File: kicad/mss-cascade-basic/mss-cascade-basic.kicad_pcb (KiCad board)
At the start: 2 copper layers, 73.7 x 38.1 mm, 36 parts, among them J1 Screw_Terminal_01x02, J2 AVR-ISP, J3 8P8C, J4 8P8C, SW1 FSM4JSMATR, T1 PE-51687, U1 AP7381-33Y, U2 INA180A4, U3 ATtiny85-20S, U4 TLP241A

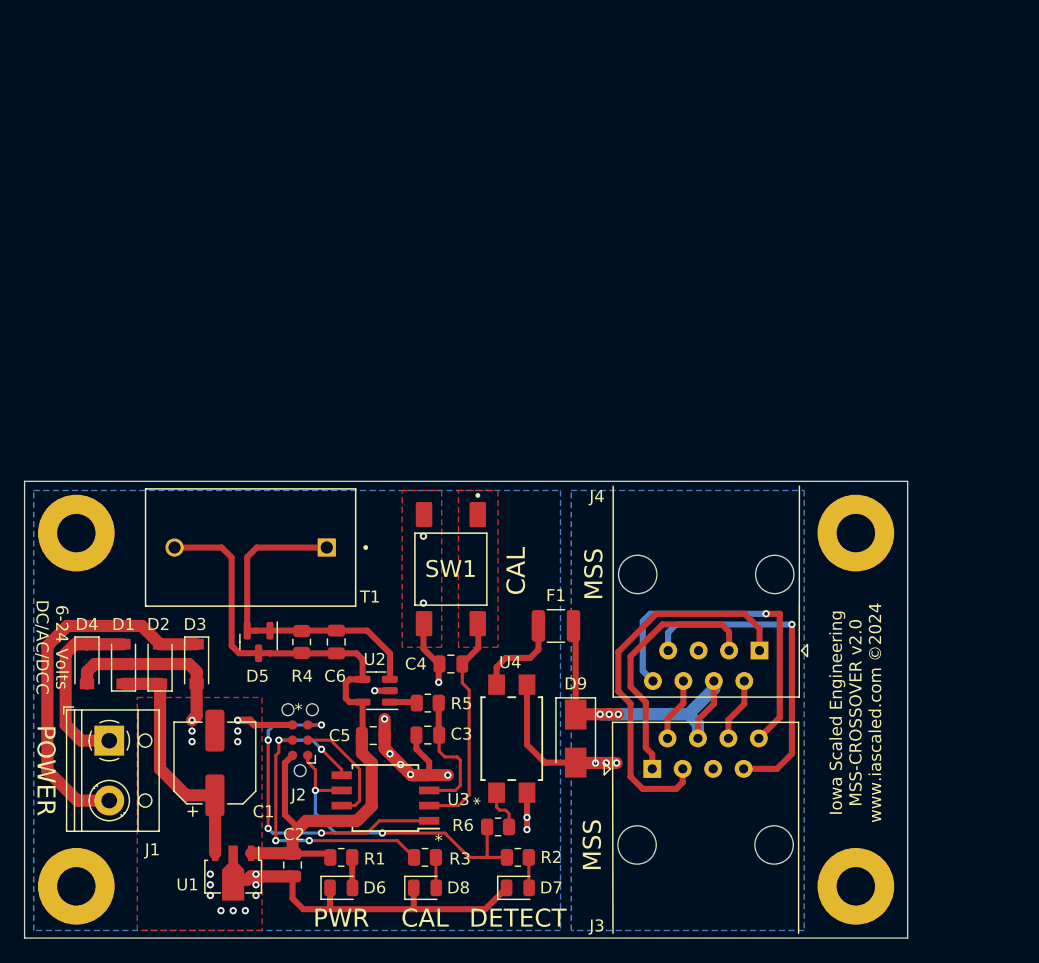
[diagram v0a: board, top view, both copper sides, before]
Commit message: Initial PCB layout for basic cascade
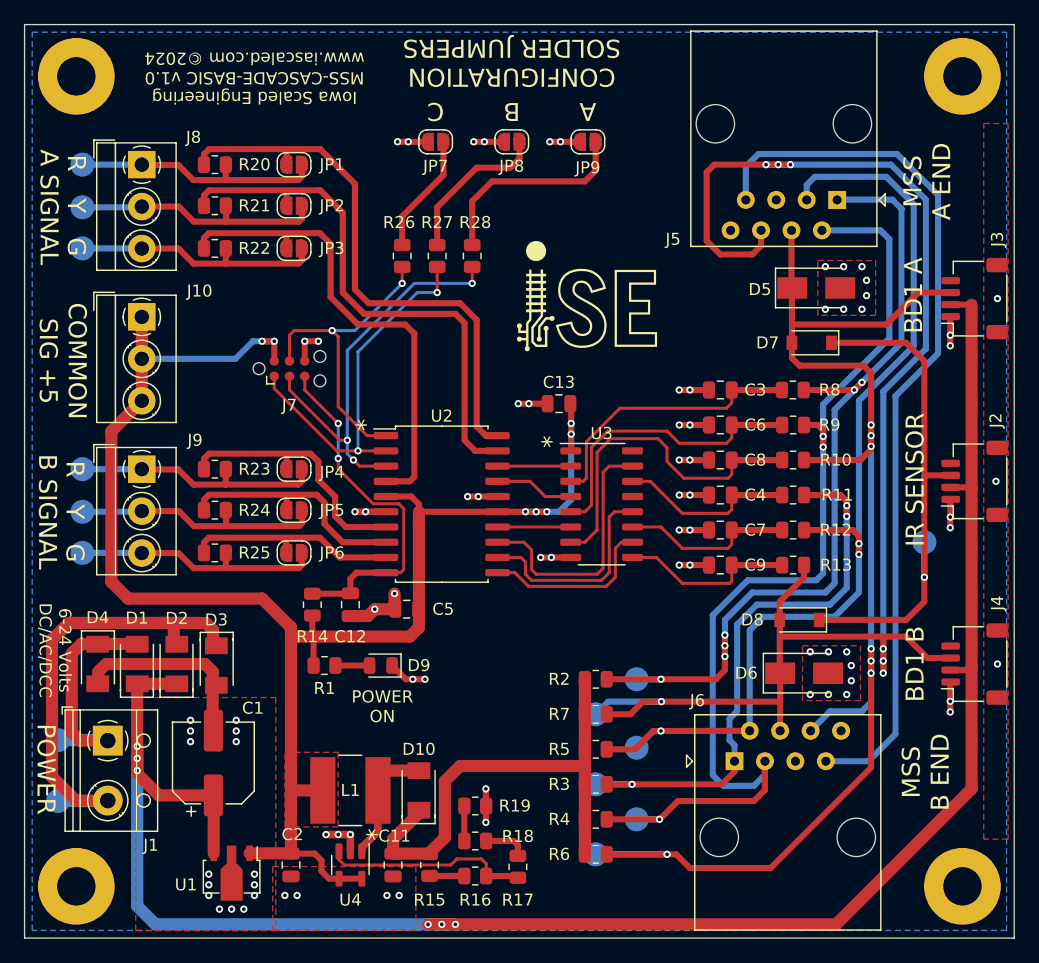
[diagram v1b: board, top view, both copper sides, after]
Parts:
- removed F1: 1210L020WR, Resistor_SMD:R_1210_3225Metric
- removed SW1: FSM4JSMATR, ISE_Generic:TE_FSM4JSMA
- removed T1: PE-51687, ISE_Generic:XFMR_PE-51687
- added C11: 10uF, Capacitor_SMD:C_0805_2012Metric, F.Cu at (56.1, 185.7)
- added C12: 1uF, Capacitor_SMD:C_0805_2012Metric, F.Cu at (52.6, 164.0)
- added C13: 0.1uF, Capacitor_SMD:C_0805_2012Metric, F.Cu at (70.0, 147.2)
- added C7: 0.1uF, Capacitor_SMD:C_0805_2012Metric, F.Cu at (83.4, 157.7)
- added C8: 0.1uF, Capacitor_SMD:C_0805_2012Metric, F.Cu at (83.4, 151.9)
- added C9: 0.1uF, Capacitor_SMD:C_0805_2012Metric, F.Cu at (83.4, 160.7)
- added D10: CDBM140G, ISE_Generic:SOD-123T, F.Cu at (58.3, 179.5)
- added J10: Screw_Terminal_01x02, TerminalBlock_MetzConnect:TerminalBlock_MetzConnect_Type059_RT06303HBWC_1x03_P3.50mm_Horizontal, F.Cu at (35.2, 140.0)
- added J5: 8P8C, Connector_RJ:RJ45_Amphenol_54602-x08_Horizontal, F.Cu at (93.2, 130.2)
- added J6: 8P8C, Connector_RJ:RJ45_Amphenol_54602-x08_Horizontal, F.Cu at (84.6, 177.0)
- added J7: AVR-ISP, Connector:Tag-Connect_TC2030-IDC-NL_2x03_P1.27mm_Vertical, F.Cu at (47.5, 144.3)
- added J8: Screw_Terminal_01x02, TerminalBlock_MetzConnect:TerminalBlock_MetzConnect_Type059_RT06303HBWC_1x03_P3.50mm_Horizontal, F.Cu at (35.2, 127.3)
- added J9: Screw_Terminal_01x02, TerminalBlock_MetzConnect:TerminalBlock_MetzConnect_Type059_RT06303HBWC_1x03_P3.50mm_Horizontal, F.Cu at (35.2, 152.7)
- added JP1: SolderJumper_2_Open, Jumper:SolderJumper-2_P1.3mm_Open_RoundedPad1.0x1.5mm, F.Cu at (47.9, 127.3)
- added JP2: SolderJumper_2_Open, Jumper:SolderJumper-2_P1.3mm_Open_RoundedPad1.0x1.5mm, F.Cu at (47.9, 130.7)
- added JP3: SolderJumper_2_Open, Jumper:SolderJumper-2_P1.3mm_Open_RoundedPad1.0x1.5mm, F.Cu at (47.9, 134.2)
- added JP4: SolderJumper_2_Open, Jumper:SolderJumper-2_P1.3mm_Open_RoundedPad1.0x1.5mm, F.Cu at (47.9, 152.7)
- added JP5: SolderJumper_2_Open, Jumper:SolderJumper-2_P1.3mm_Open_RoundedPad1.0x1.5mm, F.Cu at (47.9, 156.1)
- added JP6: SolderJumper_2_Open, Jumper:SolderJumper-2_P1.3mm_Open_RoundedPad1.0x1.5mm, F.Cu at (47.9, 159.6)
- added JP7: SolderJumper_2_Open, Jumper:SolderJumper-2_P1.3mm_Open_RoundedPad1.0x1.5mm, F.Cu at (59.7, 125.3)
- added JP8: SolderJumper_2_Open, Jumper:SolderJumper-2_P1.3mm_Open_RoundedPad1.0x1.5mm, F.Cu at (66.0, 125.3)
- added JP9: SolderJumper_2_Open, Jumper:SolderJumper-2_P1.3mm_Open_RoundedPad1.0x1.5mm, F.Cu at (72.4, 125.3)
- added L1: 4.7uH, ISE_UltraLibrarian:MSS6132-xxxMLC, F.Cu at (52.6, 179.5)
- added R10: 10k, Resistor_SMD:R_0805_2012Metric, F.Cu at (89.5, 151.9)
- added R11: 10k, Resistor_SMD:R_0805_2012Metric, F.Cu at (89.5, 154.8)
- added R12: 10k, Resistor_SMD:R_0805_2012Metric, F.Cu at (89.5, 157.7)
- added R13: 10k, Resistor_SMD:R_0805_2012Metric, F.Cu at (89.5, 160.7)
- added R14: 10k, Resistor_SMD:R_0805_2012Metric, F.Cu at (49.4, 164.0)
- added R15: 10k, Resistor_SMD:R_0805_2012Metric, F.Cu at (59.2, 185.7)
- added R16: 10k, Resistor_SMD:R_0805_2012Metric, F.Cu at (63.0, 186.6)
- added R17: 1k, Resistor_SMD:R_0805_2012Metric, F.Cu at (66.5, 185.8)
- added R18: 1k, Resistor_SMD:R_0805_2012Metric, F.Cu at (63.0, 183.7)
- added R19: 330, Resistor_SMD:R_0805_2012Metric, F.Cu at (63.0, 180.7)
- added R20: 330, Resistor_SMD:R_0805_2012Metric, F.Cu at (41.3, 127.3)
- added R21: 330, Resistor_SMD:R_0805_2012Metric, F.Cu at (41.3, 130.7)
- added R22: 330, Resistor_SMD:R_0805_2012Metric, F.Cu at (41.3, 134.2)
- added R23: 330, Resistor_SMD:R_0805_2012Metric, F.Cu at (41.3, 152.7)
- added R24: 330, Resistor_SMD:R_0805_2012Metric, F.Cu at (41.3, 156.1)
- added R25: 330, Resistor_SMD:R_0805_2012Metric, F.Cu at (41.3, 159.6)
- added R26: 1k, Resistor_SMD:R_0805_2012Metric, F.Cu at (56.9, 134.9)
- added R27: 1k, Resistor_SMD:R_0805_2012Metric, F.Cu at (59.8, 134.9)
- added R28: 1k, Resistor_SMD:R_0805_2012Metric, F.Cu at (62.7, 134.9)
- added R7: 10k, Resistor_SMD:R_0805_2012Metric, F.Cu at (73.0, 173.1)
- added R8: 10k, Resistor_SMD:R_0805_2012Metric, F.Cu at (89.5, 146.1)
- added R9: 10k, Resistor_SMD:R_0805_2012Metric, F.Cu at (89.5, 149.0)
- added TP1: TestPoint, TestPoint:TestPoint_Pad_D2.0mm, B.Cu at (100.5, 158.8)
- added TP10: TestPoint, TestPoint:TestPoint_Pad_D2.0mm, B.Cu at (73.0, 178.9)
- added TP11: TestPoint, TestPoint:TestPoint_Pad_D2.0mm, B.Cu at (76.5, 170.2)
- added TP12: TestPoint, TestPoint:TestPoint_Pad_D2.0mm, B.Cu at (76.5, 181.9)
- added TP13: TestPoint, TestPoint:TestPoint_Pad_D2.0mm, B.Cu at (73.0, 184.8)
- added TP14: TestPoint, TestPoint:TestPoint_Pad_D2.0mm, B.Cu at (73.0, 173.1)
- added TP15: TestPoint, TestPoint:TestPoint_Pad_D2.0mm, B.Cu at (76.5, 175.9)
- added TP2: TestPoint, TestPoint:TestPoint_Pad_D2.0mm, B.Cu at (30.2, 127.3)
- added TP3: TestPoint, TestPoint:TestPoint_Pad_D2.0mm, B.Cu at (30.2, 130.8)
- added TP4: TestPoint, TestPoint:TestPoint_Pad_D2.0mm, B.Cu at (30.2, 134.2)
- added TP5: TestPoint, TestPoint:TestPoint_Pad_D2.0mm, B.Cu at (30.2, 152.7)
- added TP6: TestPoint, TestPoint:TestPoint_Pad_D2.0mm, B.Cu at (30.2, 156.2)
- added TP7: TestPoint, TestPoint:TestPoint_Pad_D2.0mm, B.Cu at (30.2, 159.6)
- added TP8: TestPoint, TestPoint:TestPoint_Pad_D2.0mm, B.Cu at (28.2, 175.3)
- added TP9: TestPoint, TestPoint:TestPoint_Pad_D2.0mm, B.Cu at (28.2, 180.3)
- C3: value 1uF -> 0.1uF
- D1, D2, D3, D4: footprint Diode_SMD:D_SOD-123 -> ISE_Generic:SOD-123T
- D5: value BAV99 -> SMAJ18A-TP; footprint Package_TO_SOT_SMD:SOT-23 -> Diode_SMD:D_SMA
- D6: value GREEN LED -> SMAJ18A-TP; footprint LED_SMD:LED_0805_2012Metric -> Diode_SMD:D_SMA
- D7: value RED LED -> CDBM140G; footprint LED_SMD:LED_0805_2012Metric -> Diode_SMD:D_SOD-123
- D8: value AMBER LED -> CDBM140G; footprint LED_SMD:LED_0805_2012Metric -> Diode_SMD:D_SOD-123
- D9: value SMAJ18A-TP -> GREEN LED; footprint Diode_SMD:D_SMA -> LED_SMD:LED_0805_2012Metric
- J2: value AVR-ISP -> SM04B-SRSS; footprint Connector:Tag-Connect_TC2030-IDC-NL_2x03_P1.27mm_Vertical -> Connector_JST:JST_SH_SM04B-SRSS-TB_1x04-1MP_P1.00mm_Horizontal
- J3, J4: value 8P8C -> SM04B-SRSS; footprint Connector_RJ:RJ45_Amphenol_54602-x08_Horizontal -> Connector_JST:JST_SH_SM04B-SRSS-TB_1x04-1MP_P1.00mm_Horizontal
- R2, R3: value 1k -> 10k
- R4: value 510 -> 10k
- R5: value 100k -> 10k
- R6: value 330 -> 10k
- U1: value AP7381-33Y -> AP7381-50Y
- U2: value INA180A4 -> ATtiny861A-S; footprint Package_TO_SOT_SMD:SOT-23-5 -> Package_SO:SOIC-20W_7.5x12.8mm_P1.27mm
- U3: value ATtiny85-20S -> 74HC4049; footprint Package_SO:SOIC-8W_5.3x5.3mm_P1.27mm -> Package_SO:SO-16_3.9x9.9mm_P1.27mm
- U4: value TLP241A -> AP3012; footprint ISE_UltraLibrarian:11-5B201S_TOS -> Package_TO_SOT_SMD:SOT-23-5
- moved J2 60.3 mm to (104.6, 153.7)
- moved D5 55.1 mm to (91.4, 137.5), turned to 0 degrees
- moved D7 51.7 mm to (91.1, 142.1), turned to 180 degrees
- moved J3 47.6 mm to (104.6, 138.4), turned to 90 degrees
- moved D6 42.6 mm to (90.4, 169.7)
- moved H3 39.1 mm to (103.6, 119.9)
- moved D8 38.4 mm to (90.0, 165.2), turned to 180 degrees
- moved H4 38.1 mm to (29.7, 119.9)
- moved C3 37.7 mm to (83.4, 146.1)
- moved C6 36.8 mm to (83.4, 149.0), turned to 180 degrees
- moved U3 30.4 mm to (73.5, 155.6), turned to 0 degrees
- moved R4 28.6 mm to (73.0, 181.9), turned to 180 degrees
- moved C4 26.5 mm to (83.4, 154.8)
- moved J4 18.0 mm to (104.6, 168.9), turned to 90 degrees
- moved D9 17.4 mm to (55.1, 169.0), turned to 180 degrees
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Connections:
- C2 pad 1: +3.3V -> +5V
- C3 pad 1: /DCC_CURRENT -> Net-(C3-Pad1)
- C4 pad 1: /~{CAL_SW} -> Net-(C4-Pad1)
- C5 pad 1: +3.3V -> +5V
- C6 pad 2: +3.3V -> GND
- D5 pad 1: Net-(C6-Pad1) -> /A_ADJACENT
- D5 pad 2: Net-(C6-Pad1) -> GND
- D6 pad 1: GND -> /B_ADJACENT
- D6 pad 2: Net-(D6-Pad2) -> GND
- D7 pad 1: GND -> Net-(D7-Pad1)
- D7 pad 2: Net-(D7-Pad2) -> /A_ADJACENT
- D8 pad 1: GND -> Net-(D7-Pad1)
- D8 pad 2: Net-(D8-Pad2) -> /B_ADJACENT
- D9 pad 1: /MSS_OCC -> GND
- D9 pad 2: /MSS_GND -> Net-(D9-Pad2)
- J2 pad 1: Net-(J2-Pad1) -> GND
- J2 pad 2: +3.3V -> /VPWR
- J2 pad 3: Net-(J2-Pad3) -> Net-(D7-Pad1)
- J2 pad 4: Net-(J2-Pad4) -> unconnected-(J2-Pad4)
- J3 pad 1: Net-(J3-Pad1) -> GND
- J3 pad 2: Net-(J3-Pad2) -> /VPWR
- J3 pad 3: Net-(J3-Pad3) -> /A_ADJACENT
- J3 pad 4: /MSS_OCC -> unconnected-(J3-Pad4)
- J4 pad 1: Net-(J3-Pad3) -> GND
- J4 pad 2: Net-(J3-Pad6) -> /VPWR
- J4 pad 3: Net-(J3-Pad1) -> /B_ADJACENT
- J4 pad 4: /MSS_OCC -> unconnected-(J4-Pad4)
- R1 pad 1: Net-(D6-Pad2) -> Net-(D9-Pad2)
- R1 pad 2: +3.3V -> +5V
- R2 pad 1: Net-(J2-Pad1) -> Net-(J5-Pad1)
- R2 pad 2: Net-(D7-Pad2) -> +12V
- R3 pad 1: Net-(J2-Pad4) -> Net-(J6-Pad1)
- R3 pad 2: Net-(D8-Pad2) -> +12V
- R4 pad 1: +3.3V -> Net-(J5-Pad2)
- R4 pad 2: Net-(C6-Pad1) -> +12V
- R5 pad 1: /DCC_CURRENT -> Net-(J5-Pad3)
- R5 pad 2: Net-(R5-Pad2) -> +12V
- R6 pad 1: Net-(R6-Pad1) -> /A_ADJACENT
- R6 pad 2: Net-(J2-Pad1) -> +12V
- U1 pad 1: +3.3V -> +5V
- U2 pad 1: Net-(R5-Pad2) -> Net-(J7-Pad4)
- U2 pad 2: GND -> Net-(J7-Pad1)
- U2 pad 3: Net-(C6-Pad1) -> Net-(J7-Pad3)
- U2 pad 4: +3.3V -> /A_SIGNAL_G
- U2 pad 5: +3.3V -> +5V
- U3 pad 1: Net-(J2-Pad5) -> +5V
- U3 pad 2: /~{CAL_SW} -> /A_ADV_APPROACH_5V
- U3 pad 3: /DCC_CURRENT -> Net-(C3-Pad1)
- U3 pad 4: GND -> /A_APPROACH_5V
- U3 pad 5: Net-(J2-Pad4) -> Net-(C6-Pad1)
- U3 pad 6: Net-(J2-Pad1) -> /A_ADJACENT_5V
- U3 pad 7: Net-(J2-Pad3) -> Net-(C8-Pad1)
- U3 pad 8: +3.3V -> GND
- U4 pad 1: Net-(R6-Pad1) -> Net-(D10-Pad2)
- U4 pad 3: /MSS_GND -> Net-(R16-Pad1)
- U4 pad 4: Net-(F1-Pad2) -> +5V
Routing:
- net +5V: track 0.00 -> 140.6 mm, vias 0 -> 7
- net /VPWR: track 20.4 -> 158.5 mm, vias 0 -> 6
- net /B_ADJACENT: track 0.00 -> 128.4 mm, vias 0 -> 7
- net /A_ADJACENT: track 0.00 -> 115.5 mm, vias 0 -> 7
- net Net-(J5-Pad2): track 0.00 -> 88.0 mm, vias 0 -> 3
- net Net-(J5-Pad3): track 0.00 -> 86.0 mm, vias 0 -> 3
- net Net-(J5-Pad7): track 0.00 -> 73.8 mm
- net Net-(J5-Pad1): track 0.00 -> 72.9 mm, vias 0 -> 6
- net +3.3V: track 61.5 -> 0.00 mm
- net +12V: track 0.00 -> 55.8 mm
- net Net-(J6-Pad1): track 0.00 -> 49.2 mm, vias 0 -> 3
- net /A_SIGNAL_R: track 0.00 -> 46.9 mm
- net /A_SIGNAL_Y: track 0.00 -> 45.2 mm
- net Net-(D7-Pad1): track 0.00 -> 43.0 mm, vias 0 -> 1
- net /A_SIGNAL_G: track 0.00 -> 40.2 mm
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- added copper zone on F.Cu, net +5V
- removed copper zone on B.Cu, net /MSS_GND
- removed copper zone on F.Cu, net /~{CAL_SW}
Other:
- board size 73.7 x 38.1 mm -> 82.6 x 76.2 mm
- board text added: "A"
- board text added: "A SIGNAL"
- board text added: "B"
- board text added: "B SIGNAL"
- board text added: "BD1 A"
- board text added: "BD1 B"
- board text added: "C"
- board text added: "COMMON SIG +5"
- board text added: "CONFIGURATION SOLDER JUMPERS"
- board text added: "G"
- board text added: "IR SENSOR"
- board text added: "Iowa Scaled Engineering MSS-CASCADE-BASIC v1.0 www.iascaled.com ©2024"
- board text added: "MSS A END"
- board text added: "MSS B END"
- board text added: "POWER ON"
- board text added: "Q3"
- board text added: "R"
- board text added: "Y"
- board text added: "ZXMS6004FF"
- board text removed: "CAL"
- board text removed: "DETECT"
- board text removed: "Iowa Scaled Engineering MSS-CROSSOVER v2.0 www.iascaled.com ©2024"
- board text removed: "MSS"
- board text removed: "PWR"
